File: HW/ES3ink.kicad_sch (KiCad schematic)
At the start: 69 parts, among them J1 USB_C_Receptacle_USB2.0, J2 Conn_01x24_Pin, J2 USB_C_Receptacle_USB2.0, J3 Conn_01x02_Pin, J4 Conn_01x04_Socket, Q1 AO3401A, Q2 SI1308EDL-T1-GE3, Q3 DMP2045U-7, Q4 SI2305, SW1 RESET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

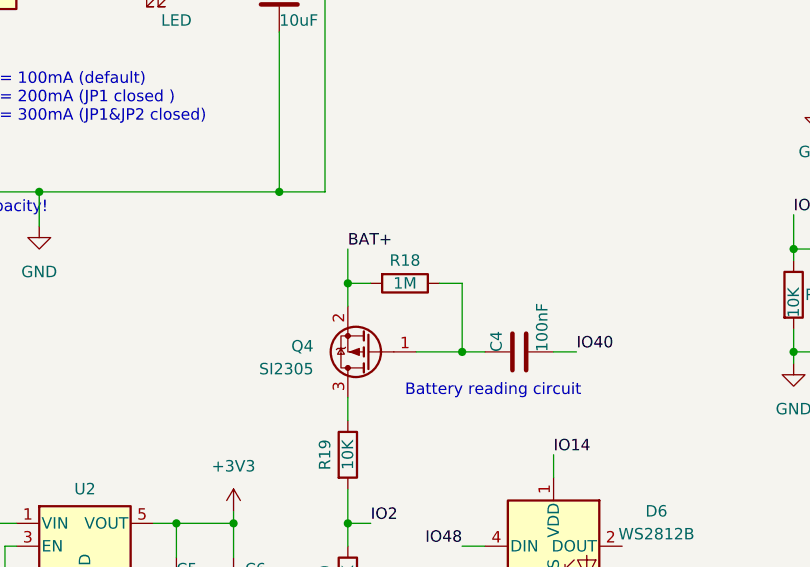
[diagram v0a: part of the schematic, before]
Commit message: Update
- changed format to KiCad 8
- changed some tracks
- add JP3 label
- add OHW logo
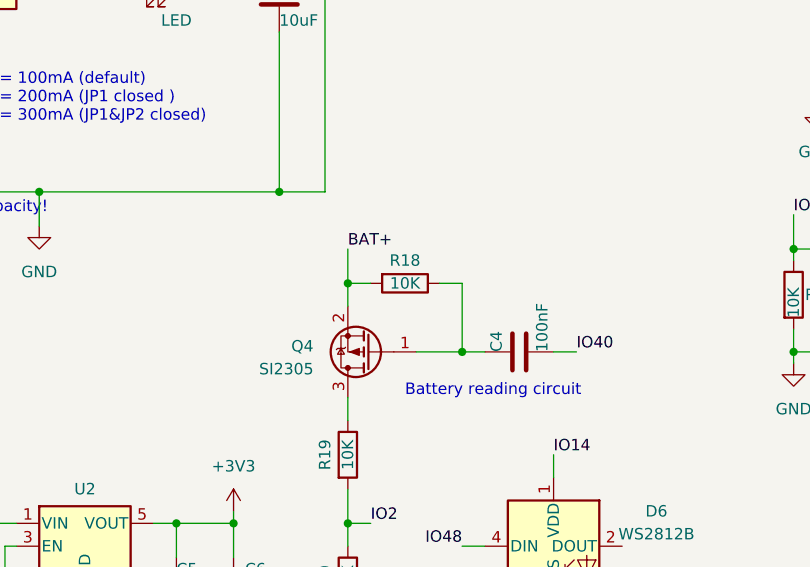
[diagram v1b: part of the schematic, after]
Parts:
- R18: value 1M -> 10K

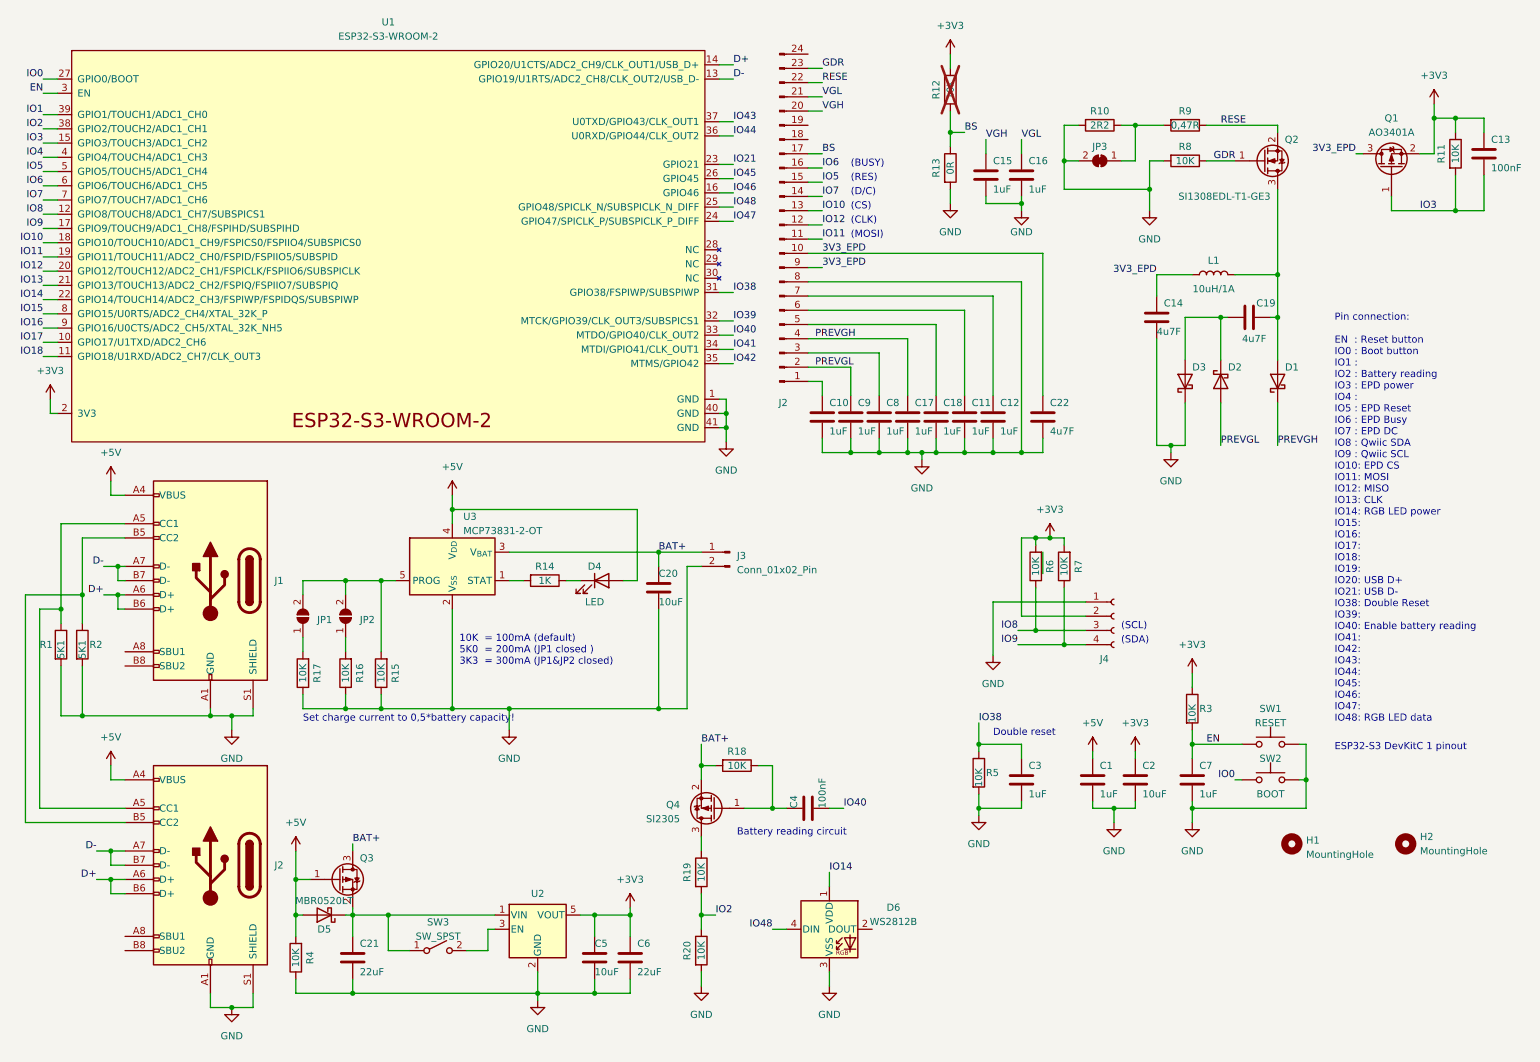
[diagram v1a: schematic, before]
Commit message: Update
- upgrade to KiCad 9
- changed U1 from ESP32-S3-WROOM-2 to WROOM-1
- added 3D models to project
- added fiducials
- changed routing of the board
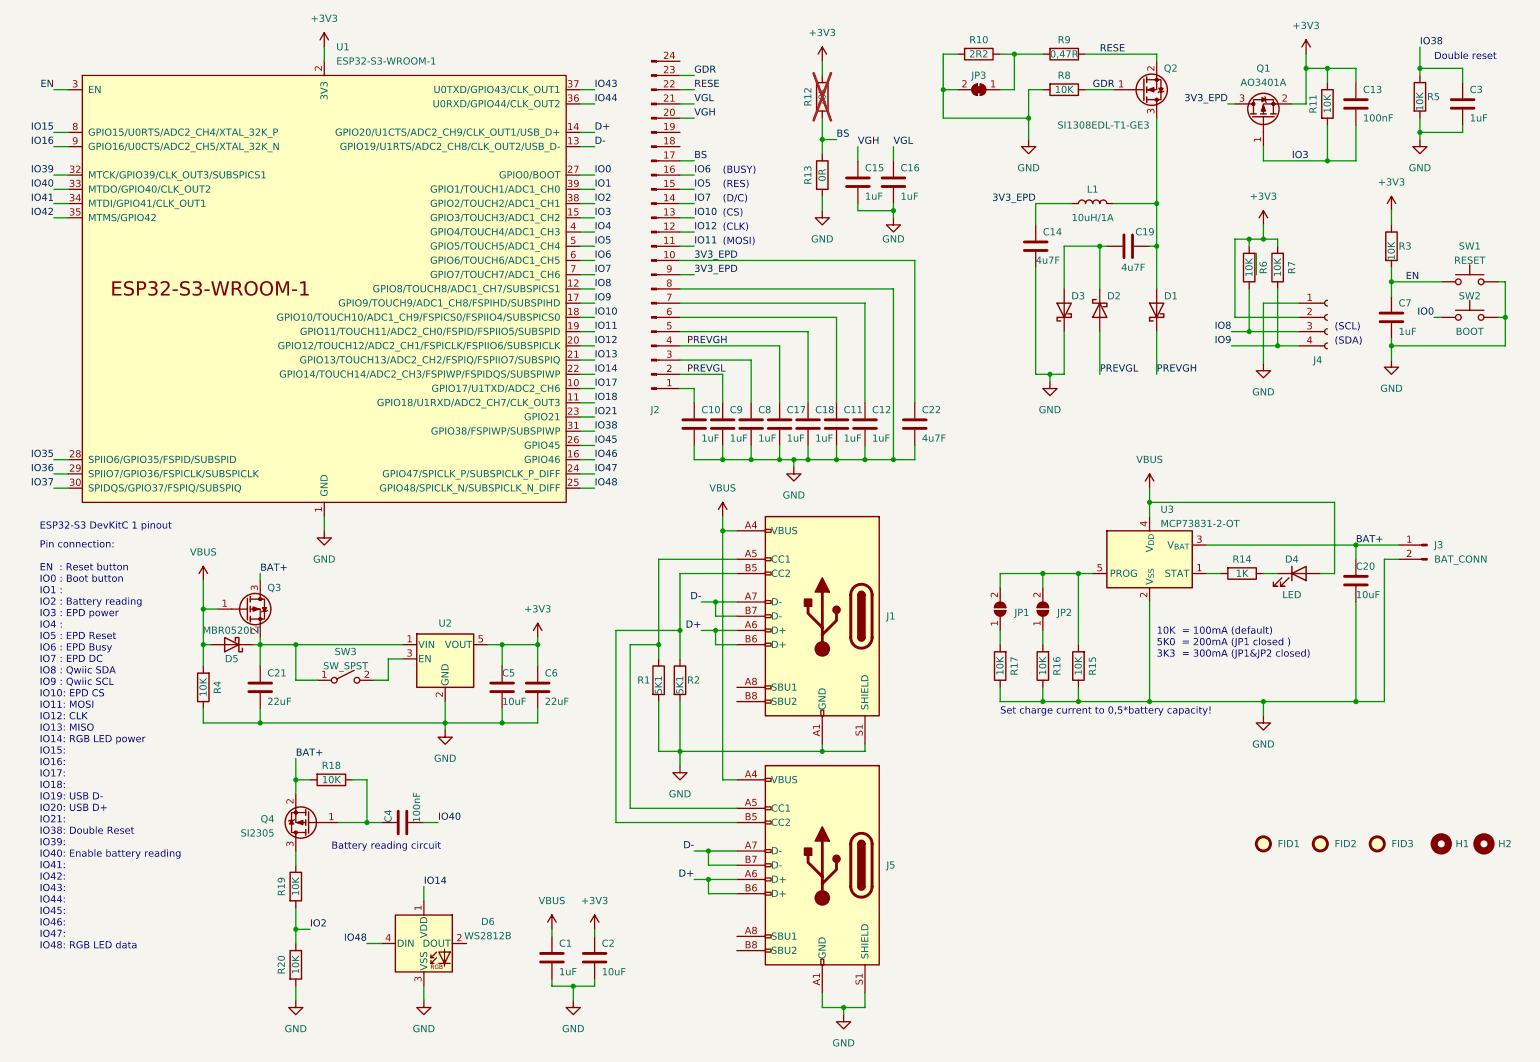
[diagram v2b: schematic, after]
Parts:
- added FID1, FID2, FID3: Fiducial, Fiducial:Fiducial_0.75mm_Mask1.5mm, symbol Mechanical:Fiducial
- J3: value Conn_01x02_Pin -> BAT_CONN
- U1: value ESP32-S3-WROOM-2 -> ESP32-S3-WROOM-1; footprint ESP32_libraries:ESP32-S3-WROOM-2 -> PCM_Espressif:ESP32-S3-WROOM-1; symbol Espressif:ESP32-S3-WROOM-2 -> PCM_Espressif:ESP32-S3-WROOM-1
- renumbered J2 to J5
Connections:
- net IO35: now reaches U1.28 (SPIIO6/GPIO35/FSPID/SUBSPID)
- net IO36: now reaches U1.29 (SPIIO7/GPIO36/FSPICLK/SUBSPICLK)
- net IO37: now reaches U1.30 (SPIDQS/GPIO37/FSPIQ/SUBSPIQ)
- net +5V renamed VBUS
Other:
- note added: "Pin connection: EN : Reset button IO0 : Boot button IO1 : IO2 : Battery reading IO3 : EPD power IO4 : IO5 : EPD Reset IO6 : EPD Busy IO7 : EPD DC IO8 : Qwiic SDA IO9 : Qwiic SCL IO10: EPD CS IO11: MOSI IO12: CLK IO13: MISO IO14: RGB LED power IO15: IO16: IO17: IO18: IO19: USB D- IO20: USB D+ IO21: IO38: Double Reset IO39: IO40: Enable battery reading IO41: IO42: IO43: IO44: IO45: IO46: IO47: IO48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"
- note removed: "Pin connection: EN : Reset button IO0 : Boot button IO1 : IO2 : Battery reading IO3 : EPD power IO4 : IO5 : EPD Reset IO6 : EPD Busy IO7 : EPD DC IO8 : Qwiic SDA IO9 : Qwiic SCL IO10: EPD CS IO11: MOSI IO12: MISO IO13: CLK IO14: RGB LED power IO15: IO16: IO17: IO18: IO19: IO20: USB D+ IO21: USB D- IO38: Double Reset IO39: IO40: Enable battery reading IO41: IO42: IO43: IO44: IO45: IO46: IO47: IO48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"
- moved on the sheet: C1, C10, C11, C12, C13, C14, C15, C16, C17, C18, C19, C2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
